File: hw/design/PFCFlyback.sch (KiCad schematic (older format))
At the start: 2 parts

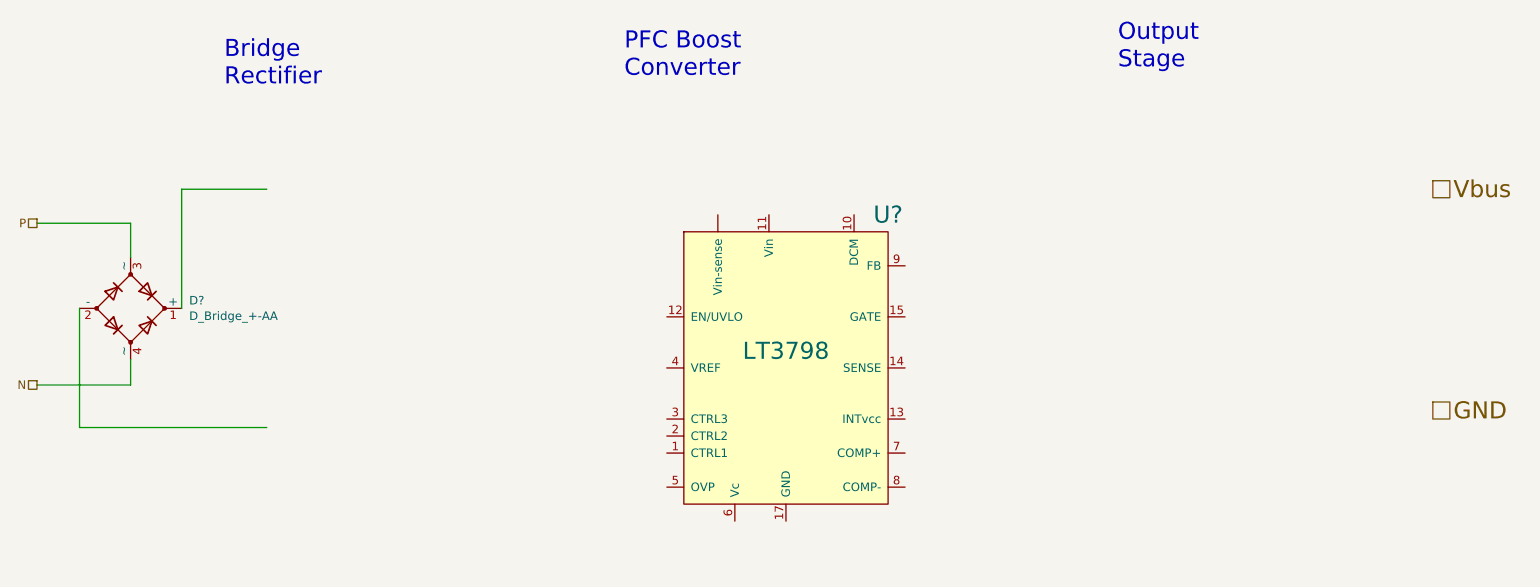
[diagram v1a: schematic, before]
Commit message: label/net reorg, primary SW starting
some reorganization of top-level naming for nets and hierarchical pins

fixed a few part selection issues

started on primary switcher sheet
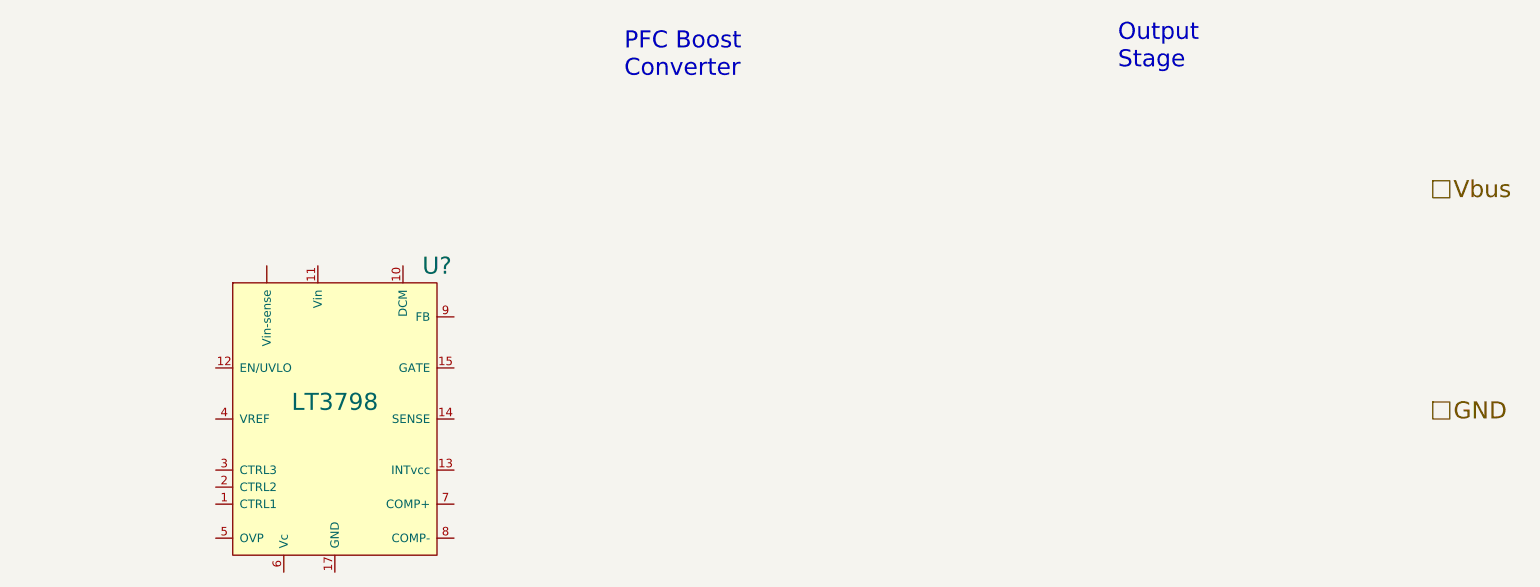
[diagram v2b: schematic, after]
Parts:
- removed D?: D_Bridge_+-AA, symbol Device:D_Bridge_+-AA
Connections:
- net labels removed: N, P
- wire segments 8 -> 0
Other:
- note removed: "Bridge\nRectifier"
- moved on the sheet: U?
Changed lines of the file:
@@
 $Descr A4 11693 8268
 encoding utf-8
-Sheet 6 7
+Sheet 6 8
 Title ""
 Date ""
@@
 Comment4 ""
 $EndDescr
-Text HLabel 1600 2300 0    50   UnSpc ~ 0
-P
-Text HLabel 1600 3250 0    50   UnSpc ~ 0
-N
-Text Notes 2700 1500 0    100  ~ 0
-Bridge\nRectifier
 Text Notes 5050 1450 0    100  ~ 0
 PFC Boost\nConverter
@@
 GND
 $Comp
-L Device:D_Bridge_+-AA D?
-U 1 1 60025329
-P 2150 2800
-F 0 "D?" H 2494 2846 50  0000 L CNN
-F 1 "D_Bridge_+-AA" H 2494 2755 50  0000 L CNN
-F 2 "" H 2150 2800 50  0001 C CNN
-F 3 "~" H 2150 2800 50  0001 C CNN
-	1    2150 2800
+L pps_klib:LT3798 U?
+U 1 1 60028304
+P 3350 3450
+F 0 "U?" H 3950 4350 100 0000 C CNN
+F 1 "LT3798" H 3350 3550 100 0000 C CNN
+F 2 "Package_SO:MSOP-16-1EP_3x4.039mm_P0.5mm_EP1.651x2.845mm" H 3350 3450 100 0001 C CNN
+F 3 "https://www.analog.com/en/products/lt3798.html" H 3350 3450 100 0001 C CNN
+	1    3350 3450
 	1    0    0    -1
 $EndComp
-Wire Wire Line
-	2150 2500 2150 2300
-Wire Wire Line
-	2150 2300 1600 2300
-Wire Wire Line
-	1600 3250 2150 3250
-Wire Wire Line
-	2150 3250 2150 3100
-Wire Wire Line
-	2450 2800 2450 2100
-Wire Wire Line
-	2450 2100 2950 2100
-Wire Wire Line
-	1850 2800 1850 3500
-Wire Wire Line
-	1850 3500 2950 3500
-$Comp
-L pps_klib:LT3798 U?
-U 1 1 60028304
-P 6000 3150
-F 0 "U?" H 6600 4050 100 0000 C CNN
-F 1 "LT3798" H 6000 3250 100 0000 C CNN
-F 2 "Package_SO:MSOP-16-1EP_3x4.039mm_P0.5mm_EP1.651x2.845mm" H 6000 3150 100 0001 C CNN
-F 3 "https://www.analog.com/en/products/lt3798.html" H 6000 3150 100 0001 C CNN
-	1    6000 3150
-	1    0    0    -1
-$EndComp
